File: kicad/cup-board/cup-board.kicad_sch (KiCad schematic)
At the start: 32 parts, among them J2 EARCUP_SPKR, J3 CUP_PWR_IN, J4 VLED_IN, J5 XF_SEC_FROM_AUDIO_BOARD, J6 SW_DRV_IN, U1 ADAU1861, U2 LSM6DSV16BX, U3 MAXM86161, U4 AQW612S, U5 AQW612S

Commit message: [LIMA] cup board: bus-powered AD2428 sub-node, on-board regulators, K2 via IO7; netlist == design file, ERC 0 errors
Co-Authored-By: Claude Opus 5.5 <noreply@anthropic.com>
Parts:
- removed J3: CUP_PWR_IN, symbol Connector_Generic:Conn_01x03
- removed J4: VLED_IN, symbol Connector_Generic:Conn_01x02
- removed J6: SW_DRV_IN, symbol Connector_Generic:Conn_01x02
- added C12: 330nF, symbol Device:C
- added C13, C27: 12pF C0G, symbol Device:C
- added C14, C15, C28: 27pF C0G, symbol Device:C
- added C16, C17, C20, C21, C24, C29, C32, C33, C34: 33nF, symbol Device:C
- added C18, C19, C30, C31: 10nF, symbol Device:C
- added C22: 470nF, symbol Device:C
- added C23, C41: 10uF 16V, symbol Device:C
- added C25: 15nF, symbol Device:C
- added C26: 3.3nF, symbol Device:C
- added C35, C37, C39, C40: 100nF, symbol Device:C
- added C36, C38: 4.7uF, symbol Device:C
- added C42: 22uF, symbol Device:C
- added C43, C45: 2.2uF 16V, symbol Device:C
- added C44, C46: 2.2uF, symbol Device:C
- added D1: ZLLS400, symbol Device:D_Schottky
- added FB1, FB2, FB3, FB4: 1000R@100MHz, symbol Device:FerriteBead
- added FL1, FL2: 2600R@100MHz CMC, symbol Filter:Choke_CommonMode_FerriteCore_1234
- added J7: A2B_A (from AeroNode / previous cup), symbol Connector_Generic:Conn_01x02
- added J8: A2B_B (to next cup), symbol Connector_Generic:Conn_01x02
- added L1, L2, L7, L8: 180nH, symbol Device:L
- added L3, L4, L5, L6: 3.3uH, symbol Device:L
- added L9: 2.2uH, symbol Device:L
- added Q1: AO3401A, symbol Transistor_FET:AO3401A
- added Q2: MMBT3904, symbol Transistor_BJT:MMBT3904
- added R10, R15, R16, R9: 120R, symbol Device:R
- added R11: 33k, symbol Device:R
- added R12: 1R 1206, symbol Device:R
- added R13: 3.3k, symbol Device:R
- added R14: 1k, symbol Device:R
- added R17: 2.2k, symbol Device:R
- added R18: 100k, symbol Device:R
- added U6: AD2428WBCPZ (sub-node), symbol AnalogDevices:AD2428
- added U7: TPS62161DSG (1V8), symbol Regulator_Switching:TPS62161DSG
- added U8: ADP7118AUJZ-3.3-R7 (3V3_MIC), symbol AnalogDevices:ADP7118
- added U9: ADP7118AUJZ-3.3-R7 (VLED), symbol AnalogDevices:ADP7118
- R7, R8: value 330 -> 220
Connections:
- net 1V8: now also C40.1, C42.1, L9.2, U6.9 (IOVDD), U7.6 (VOS)
- net 3V3_MIC: now also C44.1, U8.4 (SENSE/ADJ), U8.5 (VOUT)
- net GND: now also C12.2, C14.2, C15.2, C16.2, C17.2, C20.2, C21.2, C23.2, C24.2, C28.2, C29.2, C32.2, C33.2, C35.2, C36.2, C37.2, C38.2, C39.2, C40.2, C41.2, C42.2, C43.2, C44.2, C45.2, C46.2, L4.2, Q2.2 (E), R18.2, U6.25 (VSS), U6.31 (VSS), U6.33 (EPAD), U6.7 (ADR1/IO1), U6.8 (ADR2/IO2), U7.1 (PGND), U7.4 (AGND), U7.5 (FB), U7.9 (PAD), U8.2 (GND), U9.2 (GND); no longer U4.4 (NO_LED_K), U5.4 (NO_LED_K)
- net I2S0_BCLK: now also U6.10 (BCLK)
- net I2S0_FSYNC: now also U6.11 (SYNC)
- net I2S0_SDATAI: now also U6.12 (DTX0/IO3)
- net I2S0_SDATAO: now also U6.14 (DRX0/IO5)
- net SCL: now also U6.4 (SCL)
- net SDA: now also U6.5 (SDA)
- net VLED: now also C46.1, U9.4 (SENSE/ADJ), U9.5 (VOUT)
- net SW_DRV renamed VIN_CUP
- net VIN_CUP: now also C23.1, C35.1, C41.1, C43.1, C45.1, D1.1 (K), U6.30 (VIN), U7.2 (VIN), U7.3 (EN), U8.1 (VIN), U8.3 (EN), U9.1 (VIN), U9.3 (EN)
- new net A2B_VOUT1: C36.1, C37.1, U6.1 (PLLVDD), U6.2 (DVDD), U6.3 (DVDD), U6.32 (VOUT1)
- new net A2B_VOUT2: C38.1, C39.1, U6.20 (ATRXVDD), U6.21 (BTRXVDD), U6.29 (VOUT2)
- new net A_ACM: C12.1, FB1.2, FB2.1, U6.17 (ACM)
- new net A_AN: C13.2, FB2.2, L2.1, U6.18 (AN)
- new net A_ANF: C15.1, FL1.3, L2.2
- new net A_ANT: C19.1, FL1.4, R10.2
- new net A_AP: C13.1, FB1.1, L1.1, U6.19 (AP)
- new net A_APF: C14.1, FL1.1, L1.2
- new net A_APT: C18.1, FL1.2, R9.1
- new net A_LINE_N: C19.2, C21.1, C22.2, J7.2 (Pin_2), L4.1
- new net A_LINE_P: C18.2, C20.1, C22.1, J7.1 (Pin_1), L3.1
- new net A_TCT: C16.1, C17.1, R10.1, R9.2
- new net B_BCM: FB3.2, FB4.1, U6.24 (BCM)
- new net B_BIASP: C26.2, L5.1, Q1.3 (D), R14.1
- new net B_BN: C27.2, FB4.2, L8.1, U6.23 (BN)
- new net B_BNF: FL2.3, L8.2
- new net B_BNT: C31.1, FL2.4, R16.2
- new net B_BP: C27.1, FB3.1, L7.1, U6.22 (BP)
- new net B_BPF: C28.1, FL2.1, L7.2
- new net B_BPT: C30.1, FL2.2, R15.1
- new net B_GATE: C25.2, C26.1, Q1.1 (G), R11.2, R13.2
- new net B_LINE_N: C31.2, C33.1, C34.2, J8.2 (Pin_2), L6.1
- new net B_LINE_P: C30.2, C32.1, C34.1, J8.1 (Pin_1), L5.2
- new net B_QS: Q1.2 (S), R12.2
- new net B_SENSE: R14.2, U6.28 (SENSE)
- new net B_SWP: R13.1, U6.27 (SWP)
- new net B_TCT: C29.1, R15.2, R16.1
- new net B_VSSN: L6.2, U6.26 (VSSN)
- new net K2_B: Q2.1 (B), R17.2, R18.1
- new net K2_CTL: R17.1, U6.16 (PDMCLK/IO7)
- new net K2_SW: Q2.3 (C), U4.4 (NO_LED_K), U5.4 (NO_LED_K)
- new net SW1V8: L9.1, U7.7 (SW)
- new net V_NODE: C24.1, C25.1, D1.2 (A), L3.2, R11.1, R12.1
- no-connect marks 34 -> 38
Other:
- note added: "A2B SUB-NODE (2026-10-23, per Peter): U6 AD2428, bus-powered (AD242x DS Fig. 36; coupling per EVAL-AD2428WD1BZ sheet 2) A side J7 (from AeroNode or previous cup): line+ -> L3 -> V_NODE -> D1 -> VIN_CUP; line- -> L4 -> GND (this cup's ground is the recovered bus bias). B side J8 (to next cup, unused on the last cup): V_NODE -> R12 -> Q1 (gate: SWP via R13) -> L5 -> line+; line- -> L6 -> VSSN. SENS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"

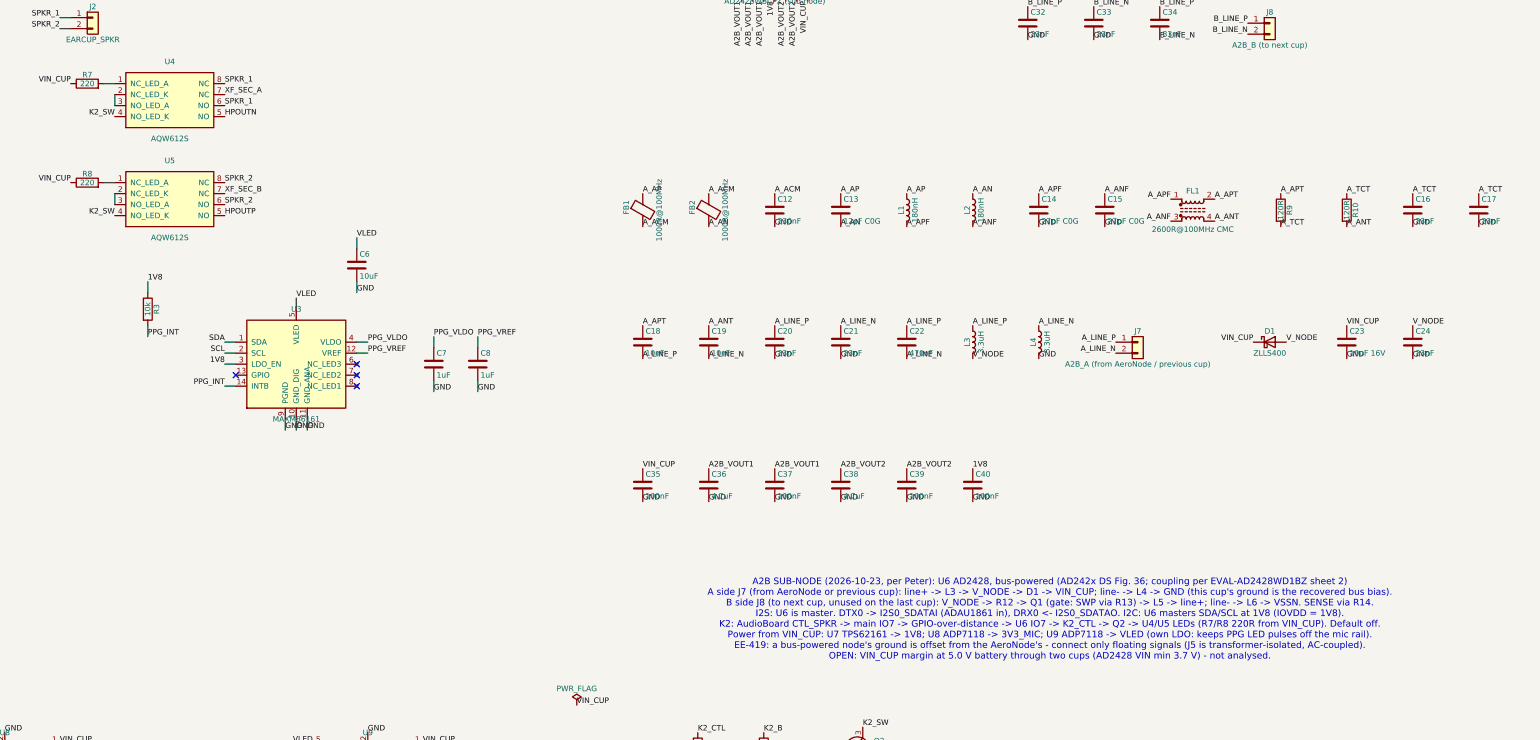
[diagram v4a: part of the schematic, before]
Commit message: [LIMA] ruling 12: 8 V A2B bus boost (LM2731X) on the audio board; cup R7/R8 680R
Co-Authored-By: Claude Opus 5.5 <noreply@anthropic.com>
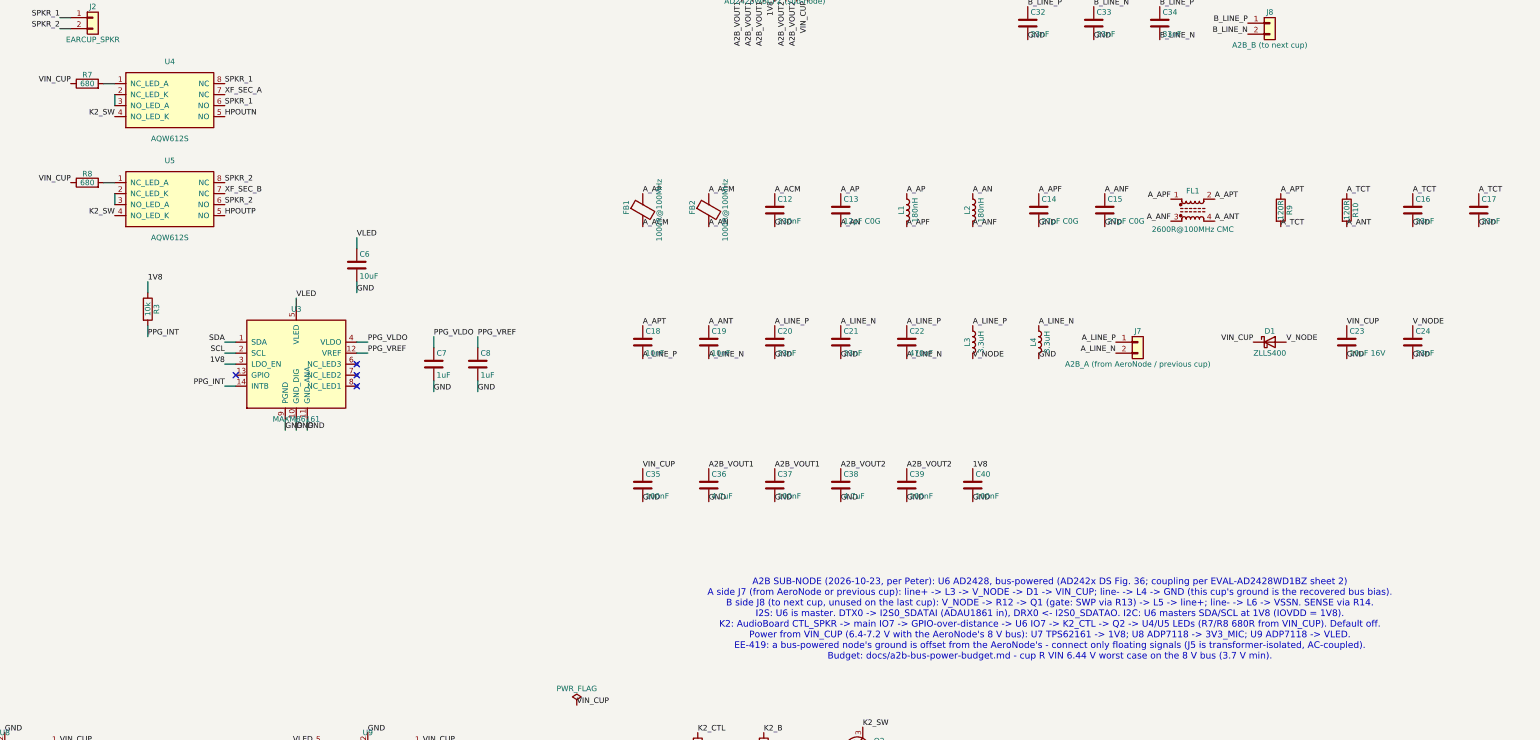
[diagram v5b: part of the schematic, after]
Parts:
- R7, R8: value 220 -> 680
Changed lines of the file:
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@@
 		)
 	)
-  (text "A2B SUB-NODE (2026-10-23, per Peter): U6 AD2428, bus-powered (AD242x DS Fig. 36; coupling per EVAL-AD2428WD1BZ sheet 2)\nA side J7 (from AeroNode or previous cup): line+ -> L3 -> V_NODE -> D1 -> VIN_CUP; line- -> L4 -> GND (this cup's ground is the recovered bus bias).\nB side J8 (to next cup, unused on the last cup): V_NODE -> R12 -> Q1 (gate: SWP via R13) -> L5 -> line+; line- -> L6 -> VSSN. SENSE via R14.\nI2S: U6 is master. DTX0 -> I2S0_SDATAI (ADAU1861 in), DRX0 <- I2S0_SDATAO. I2C: U6 masters SDA/SCL at 1V8 (IOVDD = 1V8).\nK2: AudioBoard CTL_SPKR -> main IO7 -> GPIO-over-distance -> U6 IO7 -> K2_CTL -> Q2 -> U4/U5 LEDs (R7/R8 220R from VIN_CUP). Default off.\nPower from VIN_CUP: U7 TPS62161 -> 1V8; U8 ADP7118 -> 3V3_MIC; U9 ADP7118 -> VLED (own LDO: keeps PPG LED pulses off the mic rail).\nEE-419: a bus-powered node's ground is offset from the AeroNode's - connect only floating signals (J5 is transformer-isolated, AC-coupled).\nOPEN: VIN_CUP margin at 5.0 V battery through two cups (AD2428 VIN min 3.7 V) - not analysed."
+  (text "A2B SUB-NODE (2026-10-23, per Peter): U6 AD2428, bus-powered (AD242x DS Fig. 36; coupling per EVAL-AD2428WD1BZ sheet 2)\nA side J7 (from AeroNode or previous cup): line+ -> L3 -> V_NODE -> D1 -> VIN_CUP; line- -> L4 -> GND (this cup's ground is the recovered bus bias).\nB side J8 (to next cup, unused on the last cup): V_NODE -> R12 -> Q1 (gate: SWP via R13) -> L5 -> line+; line- -> L6 -> VSSN. SENSE via R14.\nI2S: U6 is master. DTX0 -> I2S0_SDATAI (ADAU1861 in), DRX0 <- I2S0_SDATAO. I2C: U6 masters SDA/SCL at 1V8 (IOVDD = 1V8).\nK2: AudioBoard CTL_SPKR -> main IO7 -> GPIO-over-distance -> U6 IO7 -> K2_CTL -> Q2 -> U4/U5 LEDs (R7/R8 680R from VIN_CUP). Default off.\nPower from VIN_CUP (6.4-7.2 V with the AeroNode's 8 V bus): U7 TPS62161 -> 1V8; U8 ADP7118 -> 3V3_MIC; U9 ADP7118 -> VLED.\nEE-419: a bus-powered node's ground is offset from the AeroNode's - connect only floating signals (J5 is transformer-isolated, AC-coupled).\nBudget: docs/a2b-bus-power-budget.md - cup R VIN 6.44 V worst case on the 8 V bus (3.7 V min)."
     (at 475 285 0)
     (effects (font (size 1.524 1.524)))
@@
 			)
 		)
-		(property "Value" "220"
+		(property "Value" "680"
 			(at 252.73 161.29 90)
 			(effects
@@
 			)
 		)
-		(property "Value" "220"
+		(property "Value" "680"
 			(at 252.73 184.15 90)
 			(effects
